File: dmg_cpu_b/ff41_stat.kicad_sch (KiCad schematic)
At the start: 131 parts

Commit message: Fixed based on raised issues in PPU region.
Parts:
- removed PURE: INVERTER_C, symbol DMG_CPU_Cells:INVERTER_C
- SEGO, TEBY, WUGA: value TRI_INV_IF0 -> TRI_INV_IF1; symbol DMG_CPU_Cells:TRI_INV_IF0 -> DMG_CPU_Cells:TRI_INV_IF1
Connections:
- net at POFO.1 (~{ENA}), POTE.1 (~{ENA}), PUZO.1 (~{ENA})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: no longer SEGO.1 (~{ENA}), TEBY.1 (~{ENA}), WUGA.1 (~{ENA})
- net at TOBE.3, VAVE.1: now also SEGO.1 (ENA), TEBY.1 (ENA), WUGA.1 (ENA)
- net at SEGO.2: now also RUPO.2 (~{Q}); no longer RUPO.3 (Q)
- net ~{HCLK} renamed ~{YCLK}
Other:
- moved on the sheet: PAGO, ROPO, RUPO, RYJU, TOBE, VAVE

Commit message: Fixes and and rearranged schematics whereever possible to improve legibility.
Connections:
- net D0: now also SYRY.2 (D); no longer SOTA.2 (D)
- net D1: now also VUCE.2 (D); no longer SYRY.2 (D)
- net D2: now also SEDY.2 (D); no longer SALO.2 (D)
- net D3: now also SALO.2 (D); no longer SEDY.2 (D)
- net D4: now also SOTA.2 (D); no longer VEVO.2 (D)
- net D6: now also VEVO.2 (D); no longer VUCE.2 (D)
- net PX9: now also WUSA.3 (Q); no longer WUSA.2 (~{Q})
- net at SYRY.5 (Q): now also RYME.3 (2); no longer TYDE.3 (2)
- net at SYRY.6 (~{Q}): now also RETU.2; no longer VOJO.2
- net at SOTA.5 (Q): now also TYKU.3 (2); no longer RYME.3 (2)
- net at SOTA.6 (~{Q}): now also RACE.2; no longer RETU.2
- net at VEVO.5 (Q): now also TERY.3 (2); no longer TYKU.3 (2)
- net at VEVO.6 (~{Q}): now also VAFE.2; no longer RACE.2
- net at SALO.5 (Q): now also RASY.3 (2); no longer REDA.3 (2)
- net at SALO.6 (~{Q}): now also REDY.2; no longer RAZU.2
- net at SEDY.6 (~{Q}): now also RAZU.2; no longer REDY.2
- net at SEDY.5 (Q): now also REDA.3 (2); no longer RASY.3 (2)
- net at VUCE.6 (~{Q}): now also VOJO.2; no longer VAFE.2
- net at VUCE.5 (Q): now also TYDE.3 (2); no longer TERY.3 (2)
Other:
- moved on the sheet: NAPO, NYPE, PARU, POPU, SADU, SALO, SEDY, SELA, SOTA, SUKO, SYRY, TAPA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

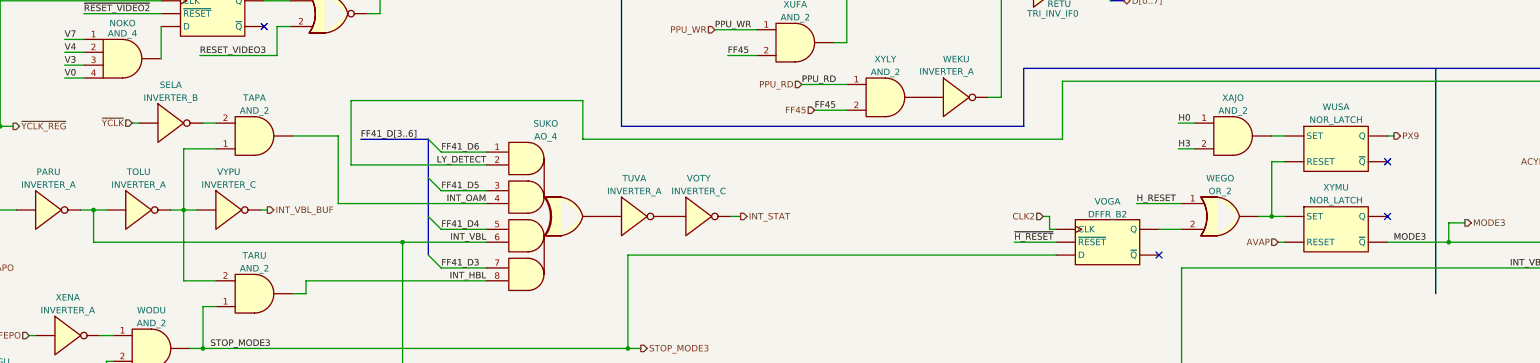
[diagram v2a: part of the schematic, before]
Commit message: BG and WIN sheets added.
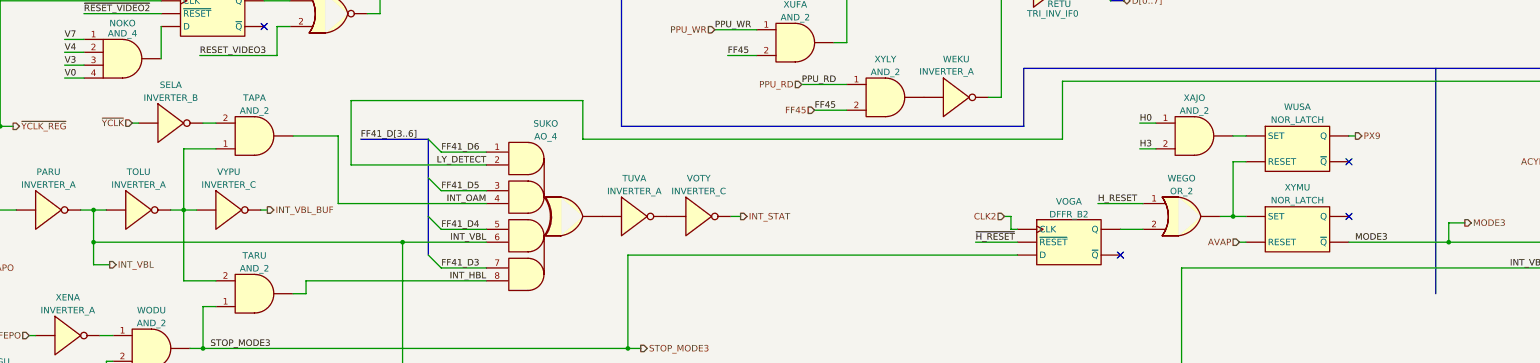
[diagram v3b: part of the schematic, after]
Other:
- moved on the sheet: VOGA, WEGO, WUSA, XAJO, XYMU

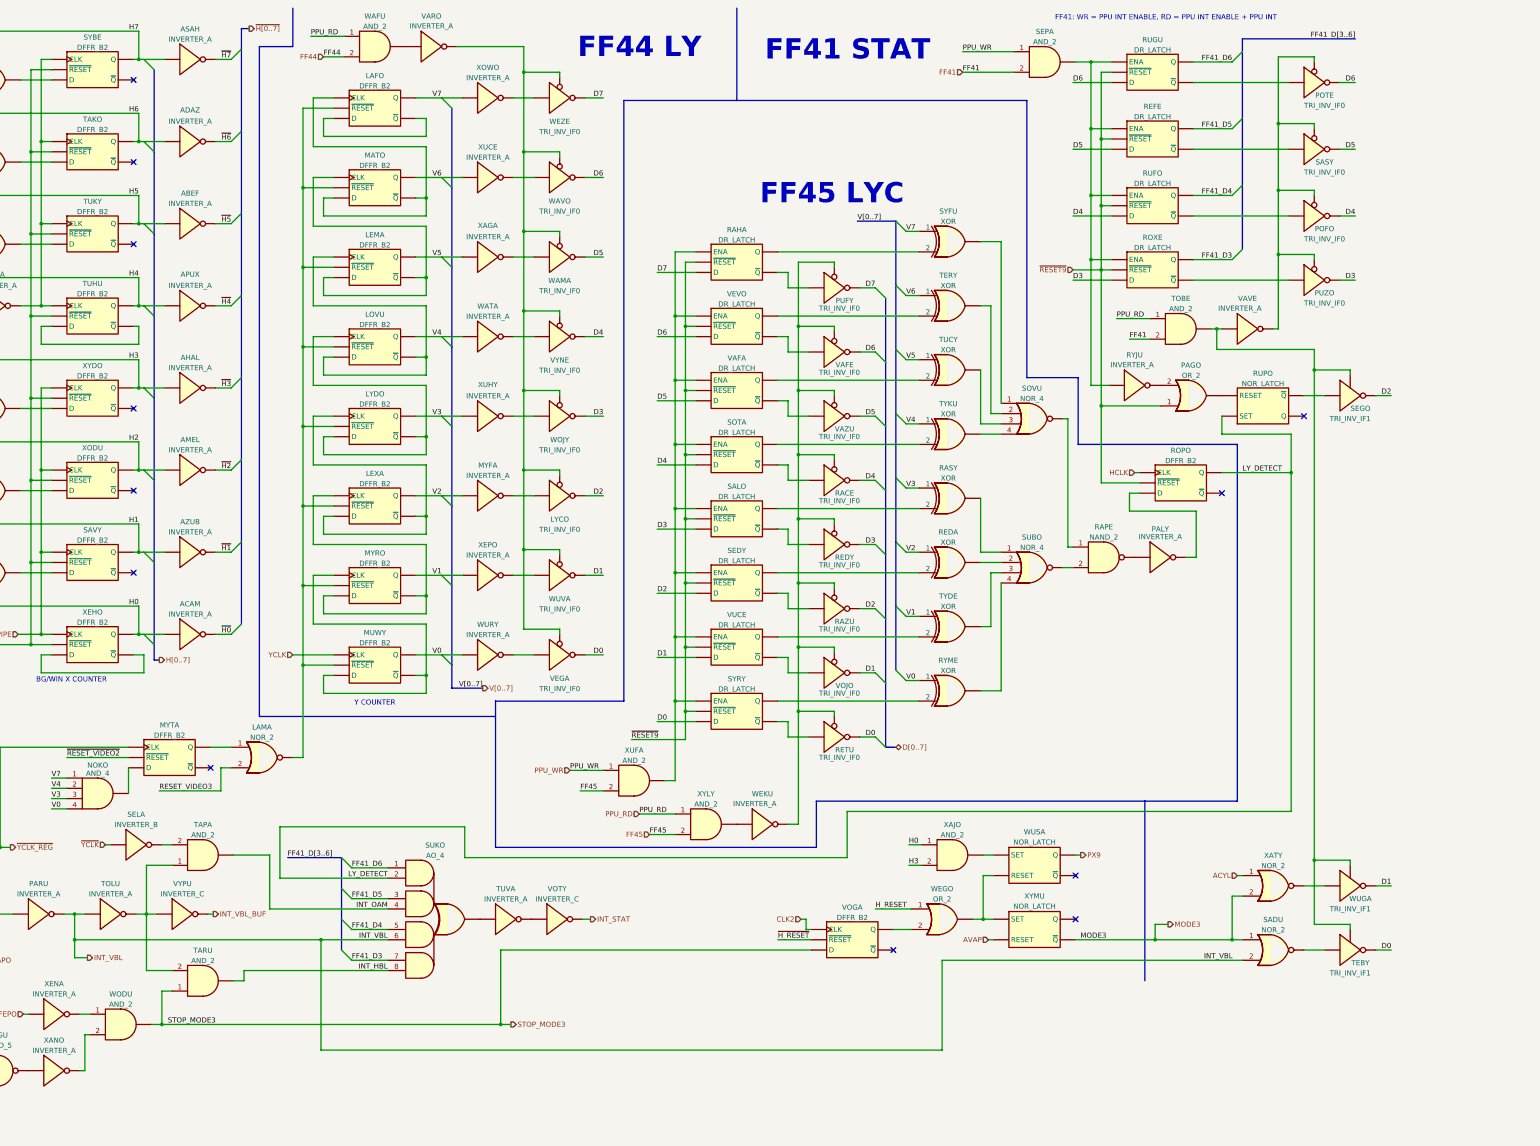
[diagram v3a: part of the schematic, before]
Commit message: VRAM interface sheet added but various edits in existing sheets. Notable merge of RESET, CLOCKS and FF04 DIV sheets
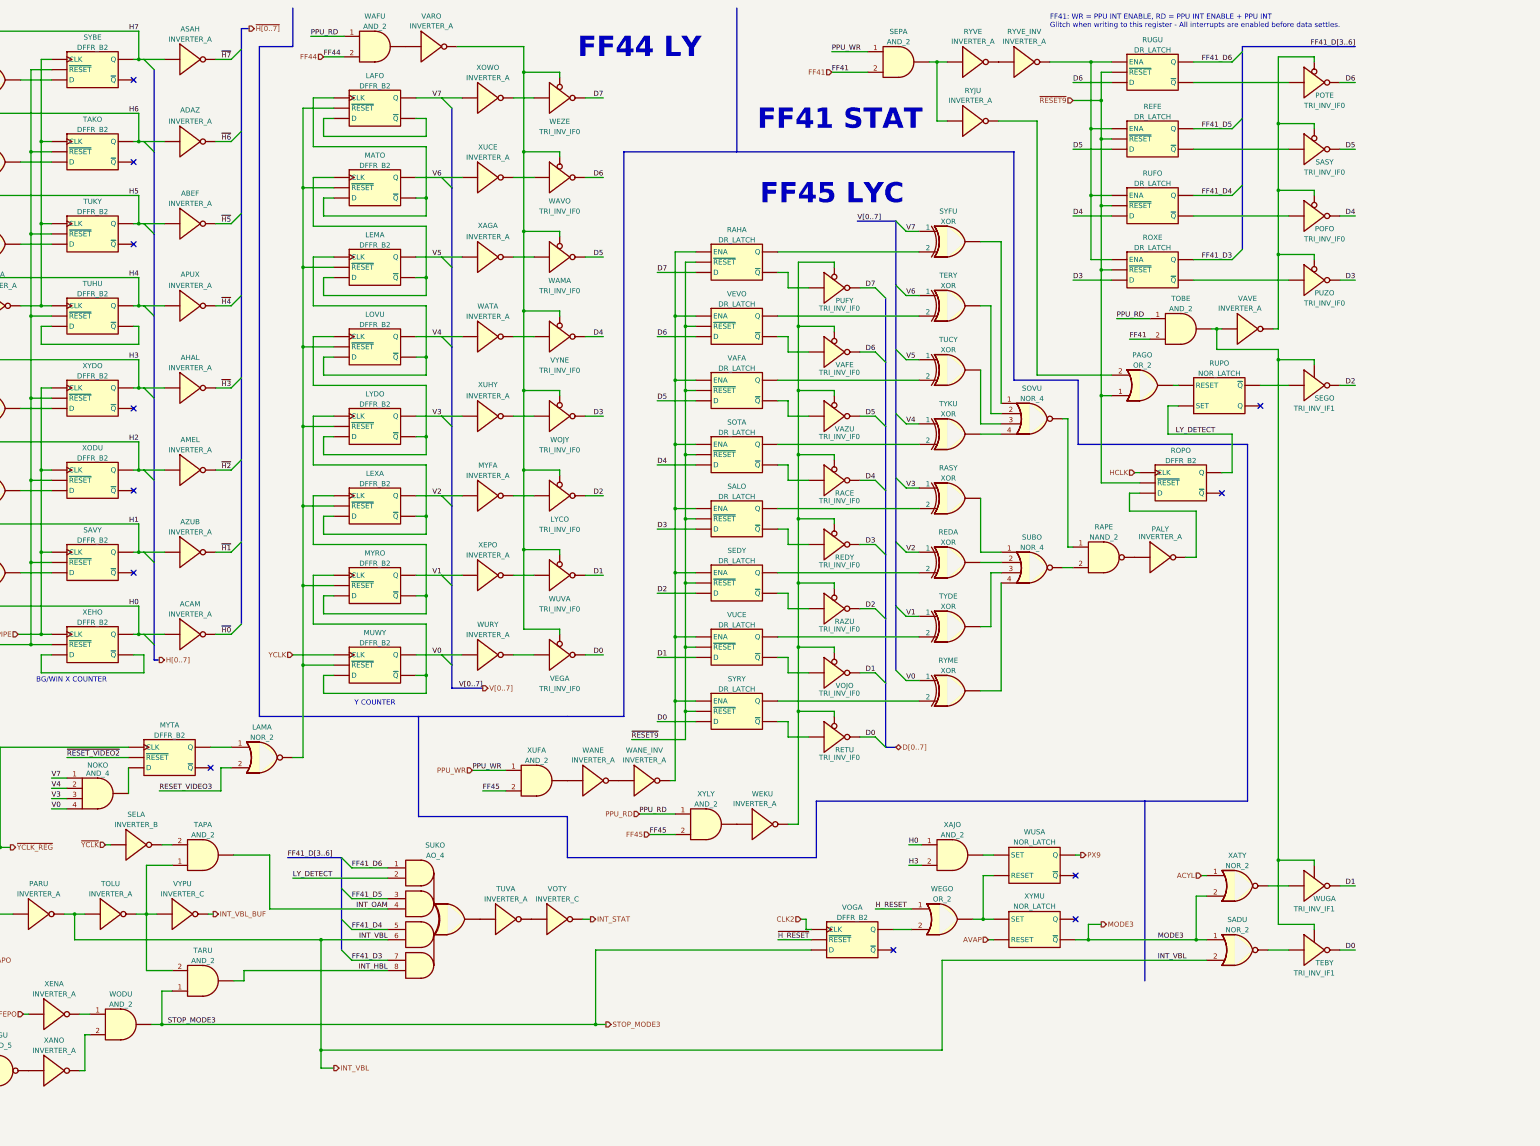
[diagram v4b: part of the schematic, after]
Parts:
- added RYVE, RYVE_INV, WANE, WANE_INV: INVERTER_A, symbol DMG_CPU_Cells:INVERTER_A
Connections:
- net at RAHA.1 (~{ENA}), RAHA.3 (ENA), SALO.1 (~{ENA})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: now also WANE_INV.2; no longer XUFA.3
- net at REFE.1 (~{ENA}), REFE.3 (ENA), ROXE.1 (~{ENA})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: now also RYVE_INV.2; no longer RYJU.1, SEPA.3
- new net: RYVE.2, RYVE_INV.1
- new net: WANE.1, XUFA.3
- new net: WANE.2, WANE_INV.1
- new net: RYJU.1, RYVE.1, SEPA.3
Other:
- note added: "FF41: WR = PPU INT ENABLE, RD = PPU INT ENABLE + PPU INT Glitch when writing to this register - All interrupts are enabled before data settles."
- note removed: "FF41: WR = PPU INT ENABLE, RD = PPU INT ENABLE + PPU INT"
- company: (none) -> CC-BY-SA-4.0 Régis Galland & Michael Singer -- Derived work from Furrtek
- title: (none) -> DMG CPU B
- moved on the sheet: PAGO, RUPO, RYJU, SADU, SEGO, SEPA, TEBY, WUGA, XATY, XUFA

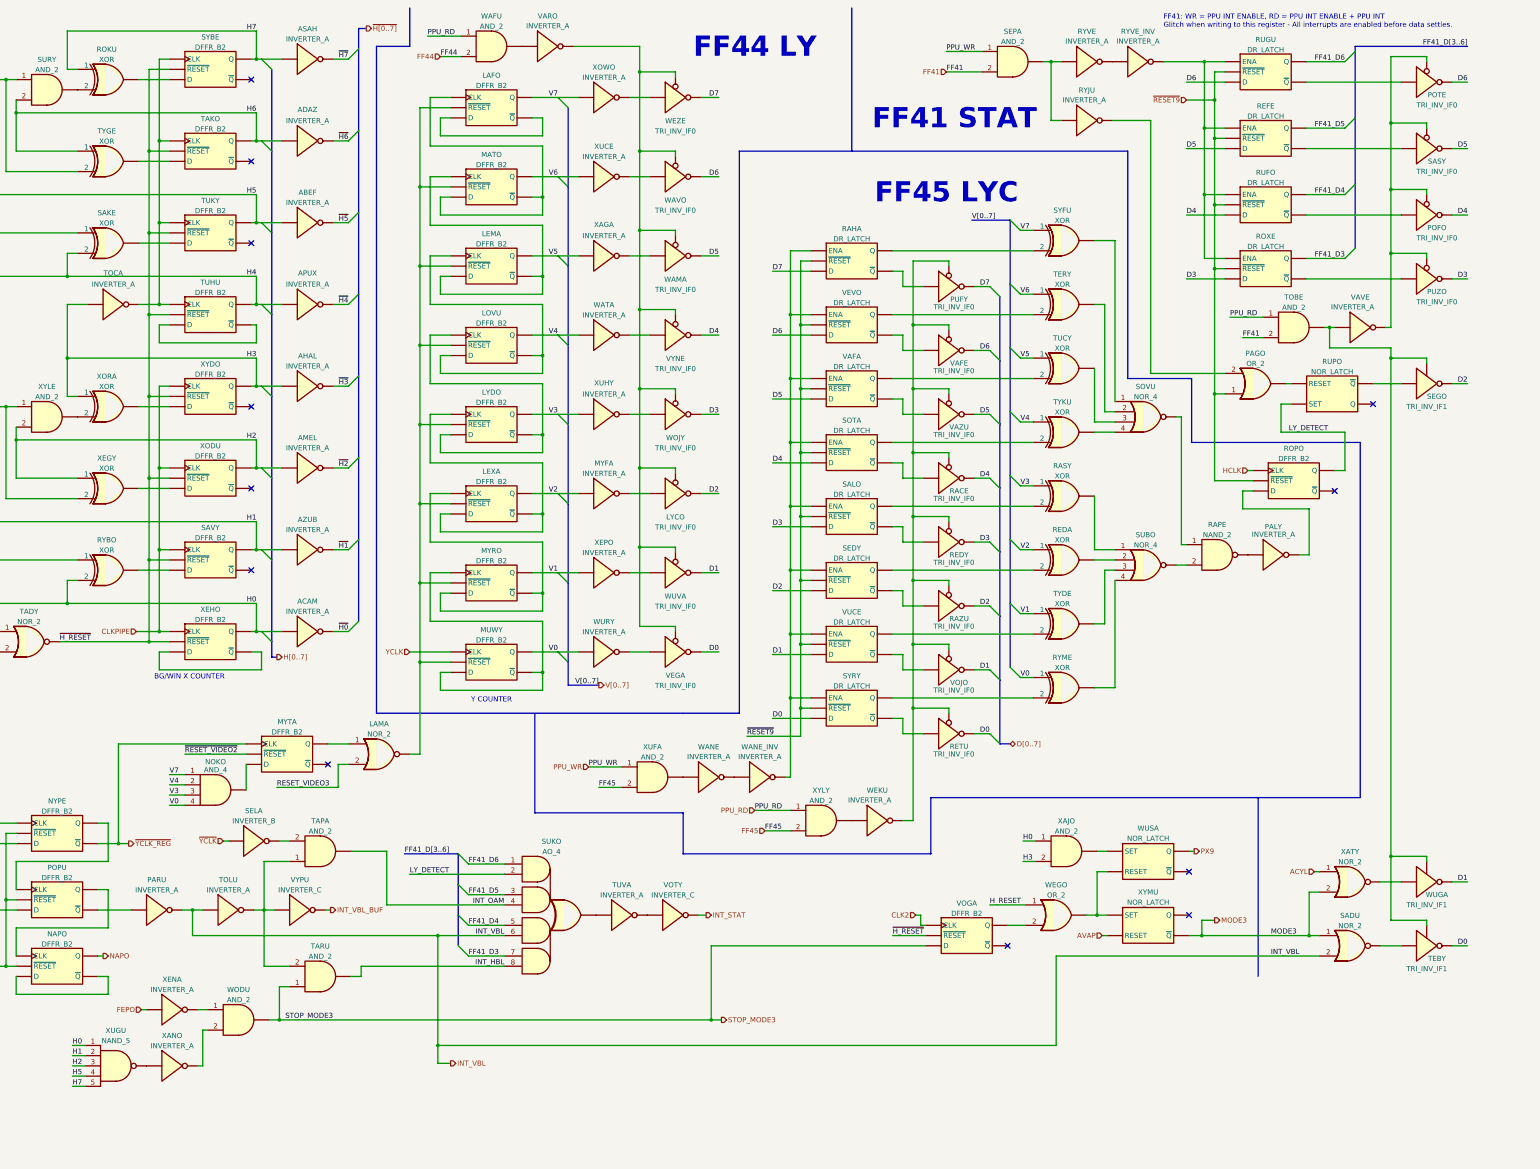
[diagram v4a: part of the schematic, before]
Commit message: Error fixed on VRAM interface page - error flwoed down from original schematics.
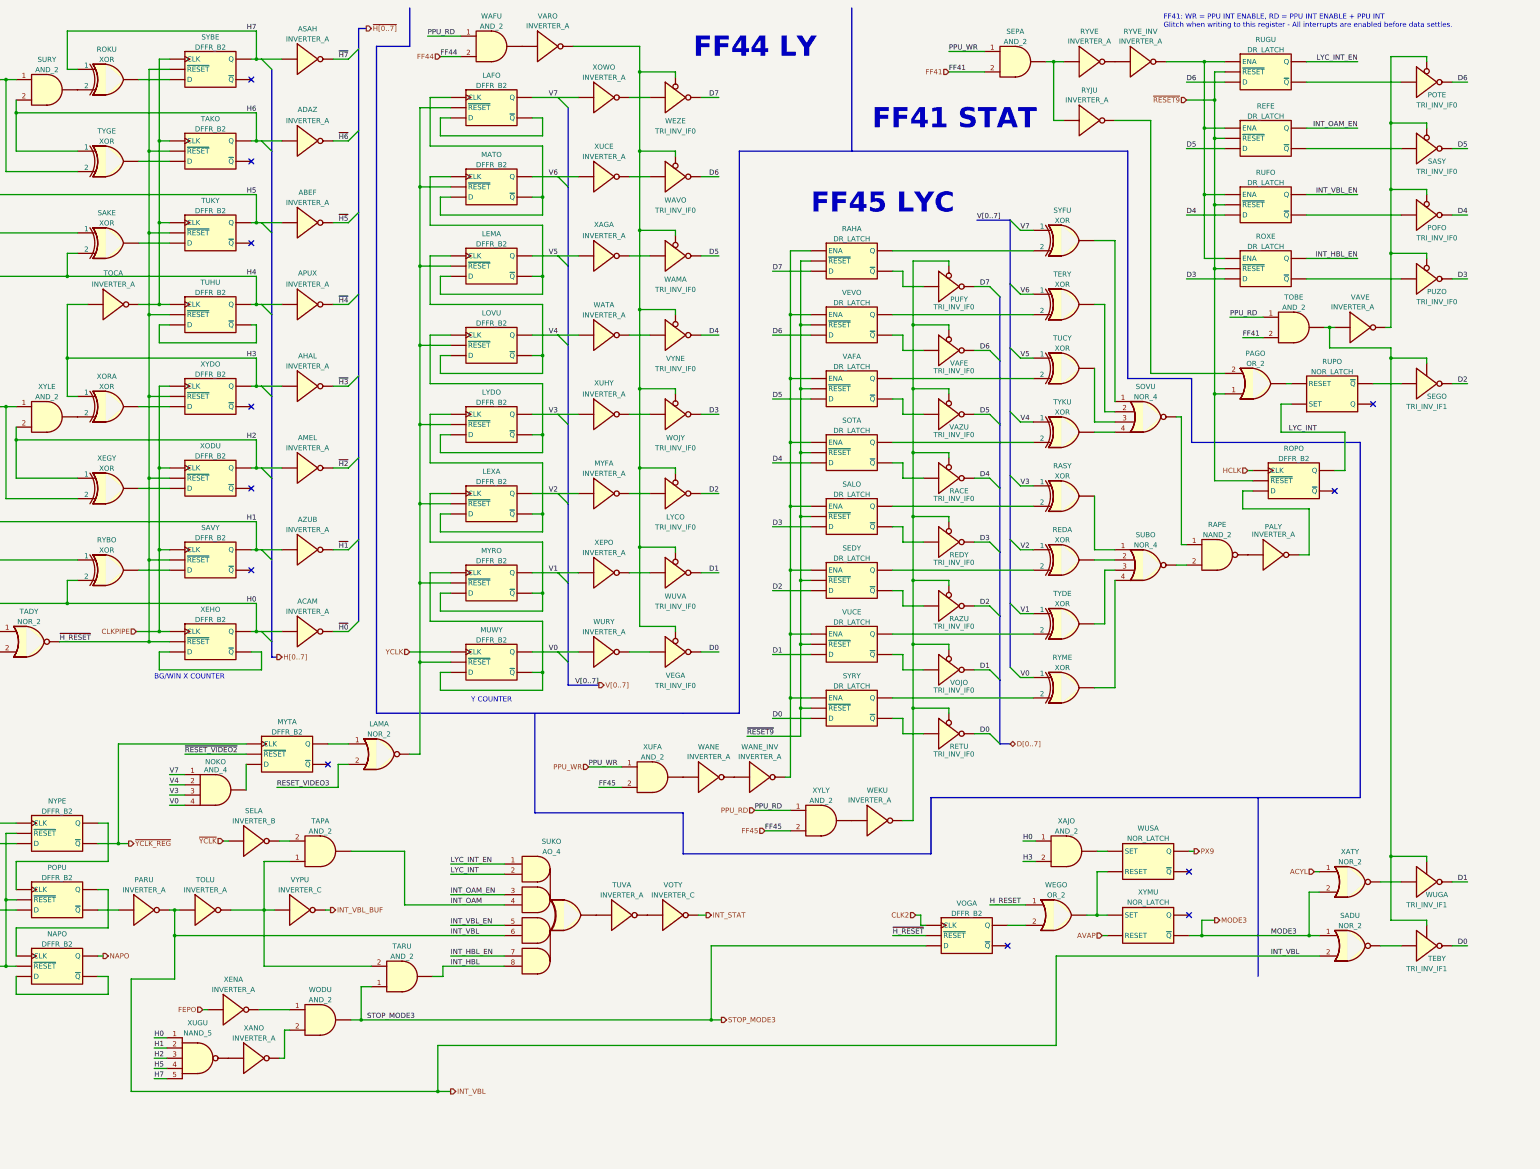
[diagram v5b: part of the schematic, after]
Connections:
- net FF41_D3 renamed INT_HBL_EN
- net FF41_D4 renamed INT_VBL_EN
- net FF41_D5 renamed INT_OAM_EN
- net FF41_D6 renamed LYC_INT_EN
- net LY_DETECT renamed LYC_INT
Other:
- moved on the sheet: PARU, RYJU, RYVE, RYVE_INV, SEPA, TARU, TOLU, WODU, XANO, XENA, XUGU
